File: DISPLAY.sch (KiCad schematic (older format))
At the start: 0 parts

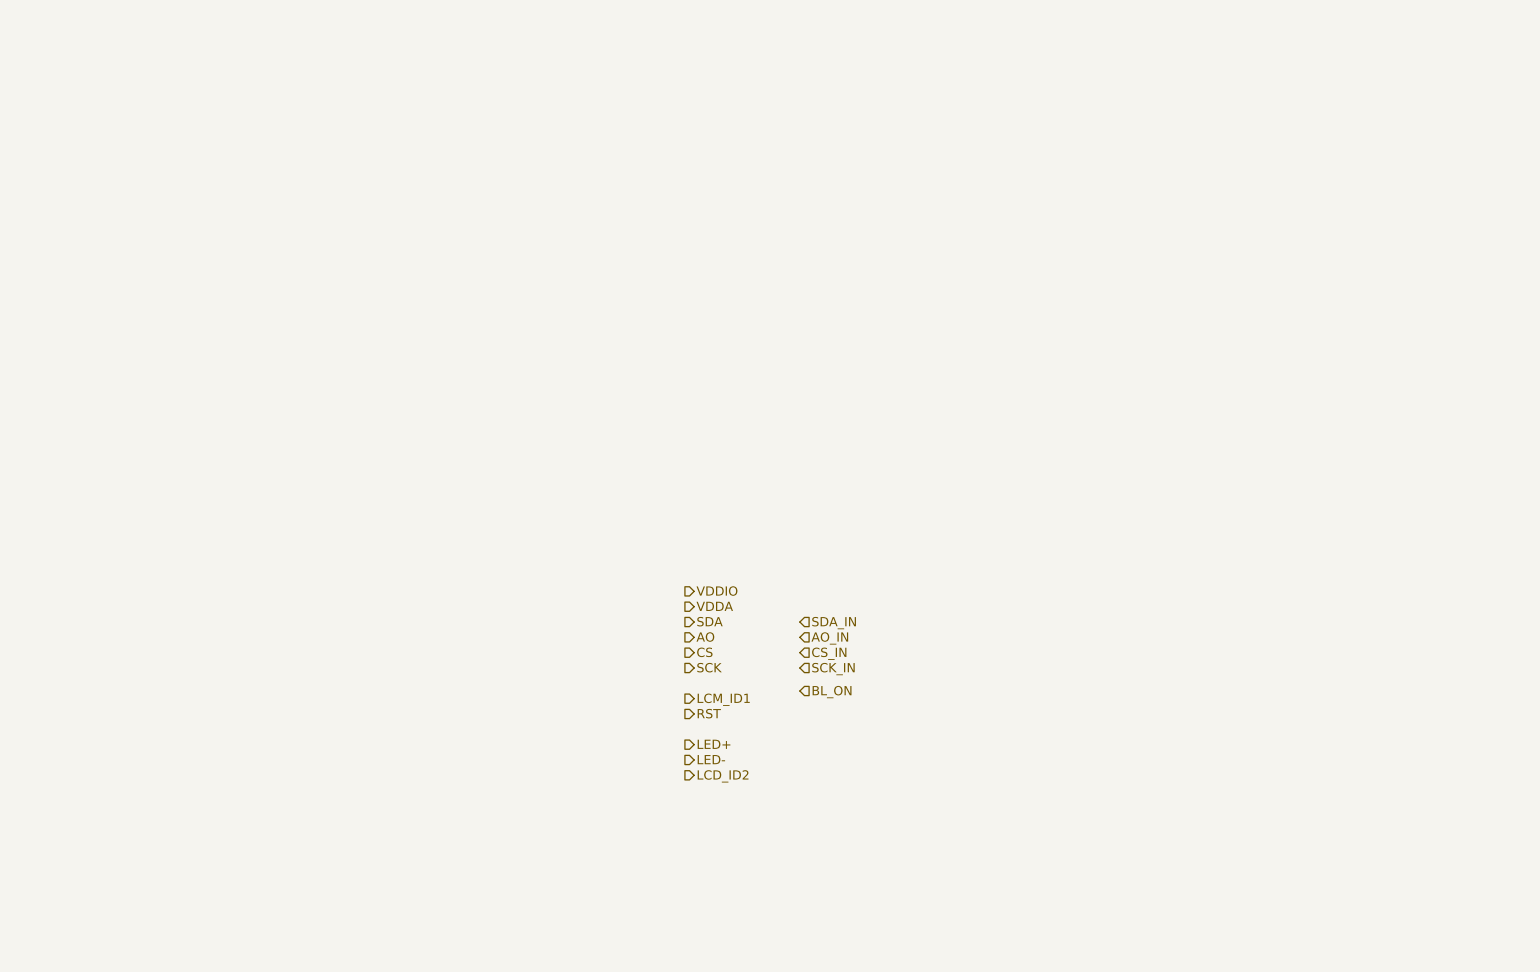
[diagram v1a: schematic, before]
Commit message: current version of the schematics. Audio circuits are still missing.
Audio curcuit topology
Audio from cellphone module is routed to STM
Audio from microphone is routed to STM
STM processes audio and routes microphone data to cellphone module
STM processes audio and routes cellphone audio to amplifier
analog multiplexer can switch route from mic directly to cellphone module and module to speaker
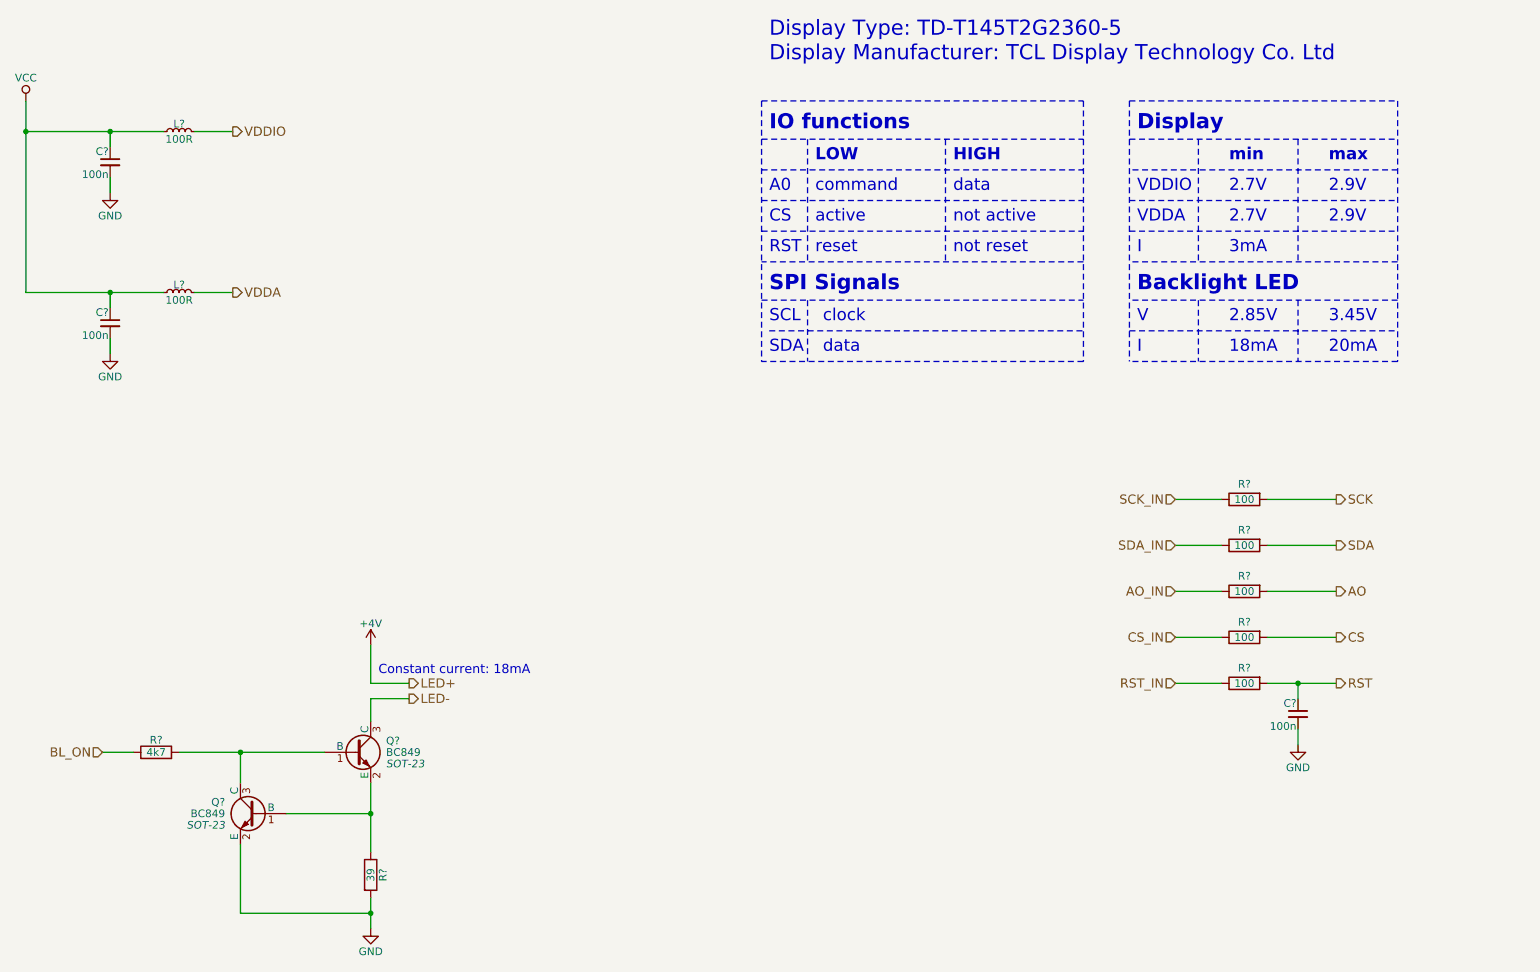
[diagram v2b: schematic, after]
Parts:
- added C? (x3): 100n, symbol C_Small
- added L? (x2): 100R, symbol L_Small
- added Q? (x2): BC849, SOT-23, symbol BC849
- added R? (x5): 100, symbol R
- added R?: 39, symbol R
- added R?: 4k7, symbol R
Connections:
- net AO: now also R?.2
- net AO_IN: now also R?.1
- net BL_ON: now also R?.1
- net CS: now also R?.2
- net CS_IN: now also R?.1
- net LED-: now also Q?.3 (C)
- net RST: now also C?.1, R?.2
- net SCK: now also R?.2
- net SCK_IN: now also R?.1
- net SDA: now also R?.2
- net SDA_IN: now also R?.1
- net VDDA: now also L?.1
- net VDDIO: now also L?.1
- new net: Q?.1 (B), Q?.3 (C), R?.2
- new net: Q?.1 (B), Q?.2 (E), R?.1
- new net GND: C?.2, C?.2, C?.2, Q?.2 (E), R?.2
- new net RST_IN: R?.1
- new net VCC: C?.1, C?.1, L?.2, L?.2
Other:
- note added: "18mA"
- note added: "2.7V"
- note added: "2.85V"
- note added: "2.9V"
- note added: "20mA"
- note added: "3.45V"
- note added: "3mA"
- note added: "A0"
- note added: "Backlight LED"
- note added: "CS"
- note added: "Constant current: 18mA"
- note added: "Display"
- note added: "Display Type: TD-T145T2G2360-5\nDisplay Manufacturer: TCL Display Technology Co. Ltd\n"
- note added: "HIGH"
- note added: "I"
- note added: "IO functions"
- note added: "LOW"
- note added: "RST"
- note added: "SCL"
- note added: "SDA"
- note added: "SPI Signals"
- note added: "V"
- note added: "VDDA"
- note added: "VDDIO"
- note added: "active"
- note added: "clock"
- note added: "command"
- note added: "data"
- note added: "max"
- note added: "min"
- note added: "not active"
- note added: "not reset"
- note added: "reset"

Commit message: added Ti WL1807/1837 Module for WLAN and Bluetooth. added Test Points
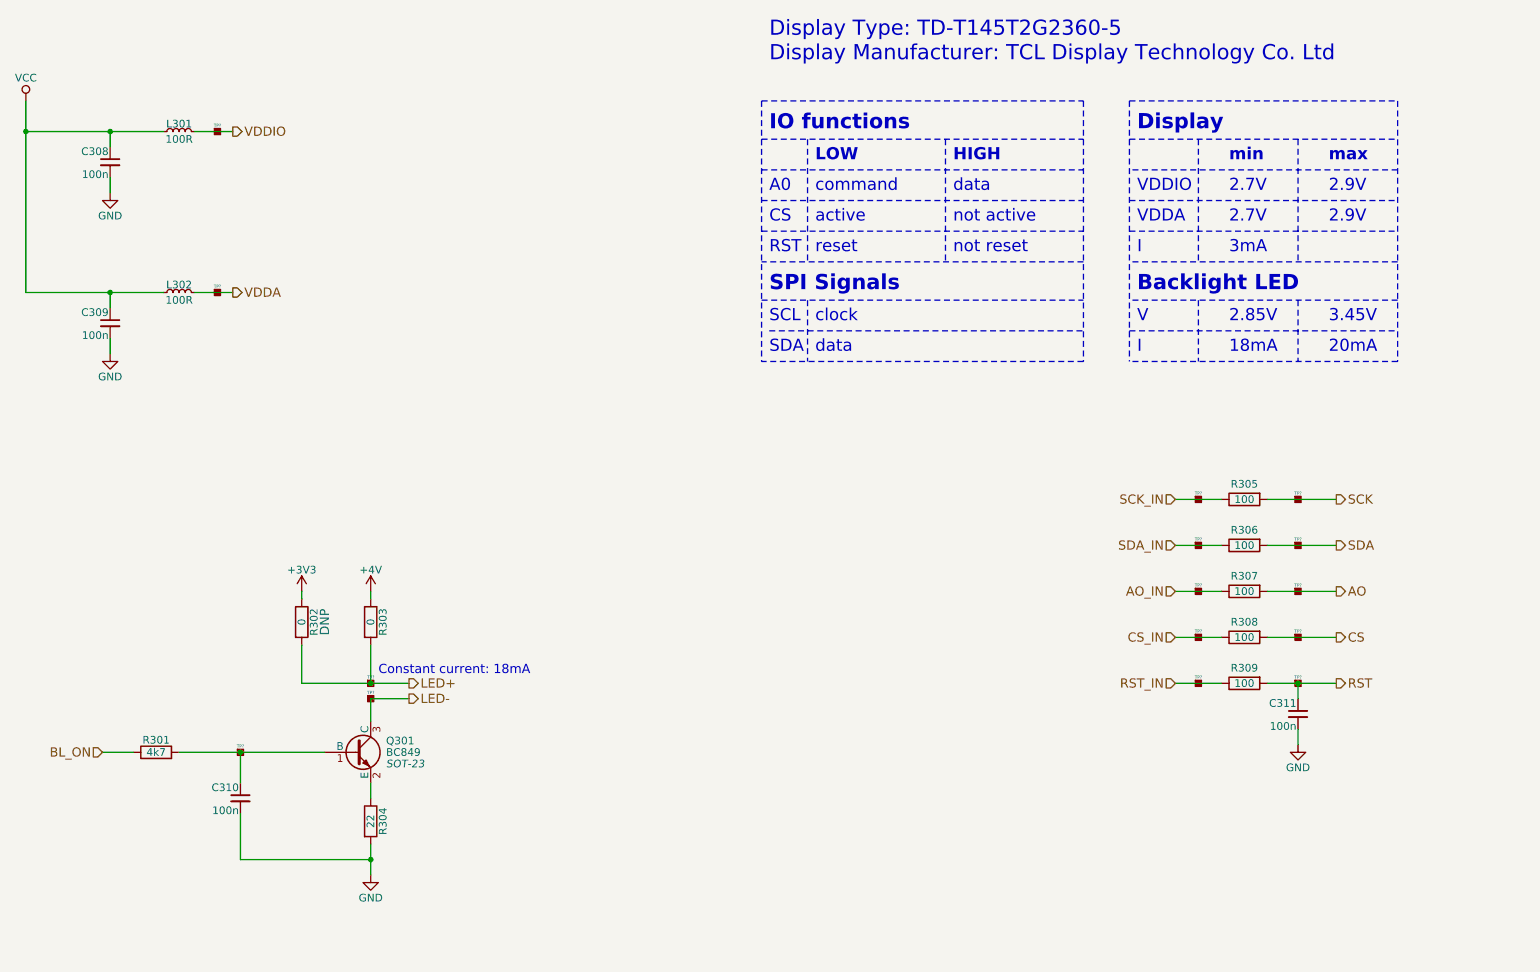
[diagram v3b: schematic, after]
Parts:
- removed Q?: BC849, SOT-23, symbol BC849
- added C310: 100n, symbol C_Small
- added R302, R303: 0, symbol R
- added TP? (x15): TP, symbol TP
- R304: renamed from R?; value 39 -> 22
- gave numbers to parts that had none: 12
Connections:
- net +4V: now also R303.1
- net GND: now also C310.2
- net LED-: now also TP?.1
- net RST: now also TP?.1
- net at Q301.1 (B), R301.2: now also C310.1, TP?.1
- new net +3V3: R302.1
- new net LED+: R302.2, R303.2, TP?.1
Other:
- moved on the sheet: R304

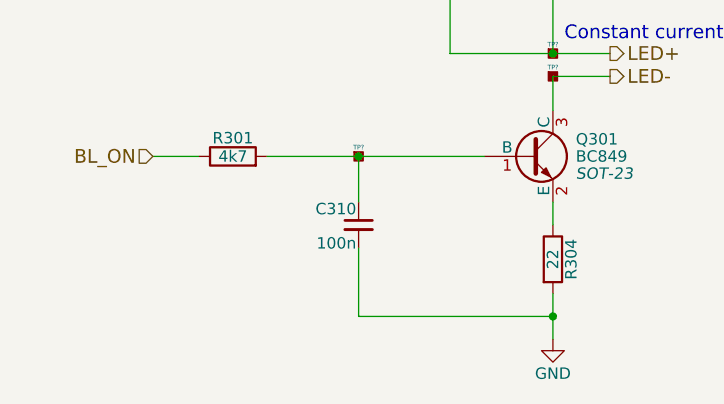
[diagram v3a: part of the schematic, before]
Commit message: short schematics review and proposed changes
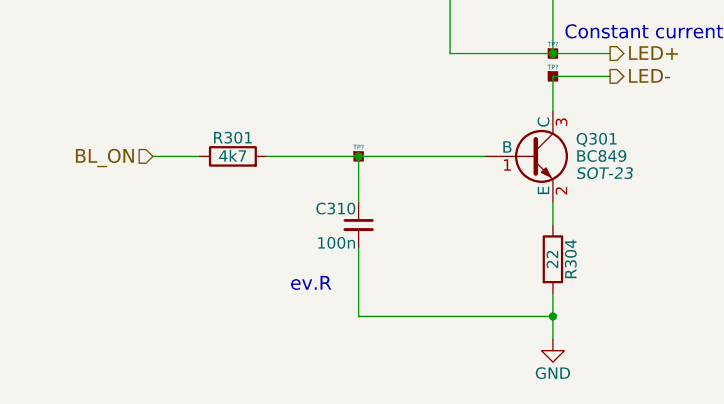
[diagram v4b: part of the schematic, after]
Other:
- note added: "ev.R"
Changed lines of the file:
@@
 	1    0    0    -1
 $EndComp
+Text Notes 2600 6450 0    60   ~ 0
+ev.R
 $EndSCHEMATC

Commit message: aktuelle Version
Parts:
- C308, C309, C310, C311: footprint (none) -> Capacitors_SMD:C_0603
- L301, L302, R301, R302, R303, R304, R305, R306, R307, R308, R309: footprint (none) -> Resistors_SMD:R_0603
- Q301: footprint SOT-23 -> TO_SOT_Packages_SMD:SOT-23
- TP301, TP302, TP303, TP304, TP305, TP306, TP307, TP308, TP309, TP310, TP311, TP312, TP313, TP314, TP315: renamed from TP?; footprint (none) -> buttons:TP
